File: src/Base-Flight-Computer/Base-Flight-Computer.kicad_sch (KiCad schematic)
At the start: 62 parts, among them J1 Jumper_NO, P1 1984659, P2 USB, P3 0530470610, P4 1546551-2, P5 1984659, Q1 QS5U17TR, Q2 2N7002W-7-F, Q3 2N7002W-7-F, Q4 QS5U17TR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

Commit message: updated symbol footprint links in schematic
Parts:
- BZ1: footprint Flight-Computer:AT-1438-TWT-R -> Base-Flight-Computer:AT-1438-TWT-R
- D1: footprint (none) -> Base-Flight-Computer:CLMVC-FKA-CL1D1L71BB7C3C3
- J1: footprint Engine-Controller:Jumper-NO -> Base-Flight-Computer:Jumper-NO
- P2: footprint Flight-Computer-Lite:10118194-0001LF -> Base-Flight-Computer:10118194-0001LF
- P3: footprint Flight-Computer-Lite:3220-20-0200-00 -> Base-Flight-Computer:53047-0610
- P4: footprint Flight-Computer:1546551-2 -> Base-Flight-Computer:1546551-2
- P5: footprint Base-Flight-Computer:JST_S2B-PH-K-S(LF)(SN) -> Base-Flight-Computer:1984659
- Q1, Q4: footprint Flight-Computer:QS5U17TR -> Base-Flight-Computer:QS5U17TR
- Q2, Q5, Q6: footprint Flight-Computer-Lite:QS5U17TR -> Base-Flight-Computer:2N7002W-7-F
- Q3: footprint Flight-Computer-Lite:QS5U17TR -> Base-Flight-Computer:QS5U17TR
- U1: footprint (none) -> Base-Flight-Computer:STM32G4A1KEU6
- U2: footprint (none) -> Base-Flight-Computer:BMP390
- U4: footprint (none) -> Base-Flight-Computer:SST25VF040B-50-4I-S2AE-T
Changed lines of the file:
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@@
       (effects (font (size 1.27 1.27)) (justify left) hide)
     )
-    (property "Footprint" "Flight-Computer-Lite:QS5U17TR" (at 221.361 58.293 0)
+    (property "Footprint" "Base-Flight-Computer:2N7002W-7-F" (at 221.361 58.293 0)
       (effects (font (size 1.27 1.27) italic) (justify left) hide)
     )
@@
       (effects (font (size 1.27 1.27)) (justify left) hide)
     )
-    (property "Footprint" "Flight-Computer-Lite:QS5U17TR" (at 270.637 59.182 0)
+    (property "Footprint" "Base-Flight-Computer:2N7002W-7-F" (at 270.637 59.182 0)
       (effects (font (size 1.27 1.27) italic) (justify left) hide)
     )
@@
       (effects (font (size 1.27 1.27)))
     )
-    (property "Footprint" "" (at 52.578 112.268 0)
+    (property "Footprint" "Base-Flight-Computer:BMP390" (at 52.578 112.268 0)
       (effects (font (size 1.27 1.27)) (justify left bottom) hide)
     )
@@
       (effects (font (size 1.524 1.524)) hide)
     )
-    (property "Footprint" "" (at 32.893 25.273 0)
+    (property "Footprint" "Base-Flight-Computer:STM32G4A1KEU6" (at 32.893 25.273 0)
       (effects (font (size 1.27 1.27) italic) hide)
     )
@@
       (effects (font (size 1.524 1.524)) hide)
     )
-    (property "Footprint" "Base-Flight-Computer:JST_S2B-PH-K-S(LF)(SN)" (at 31.115 166.37 0)
+    (property "Footprint" "Base-Flight-Computer:1984659" (at 31.115 166.37 0)
       (effects (font (size 1.524 1.524)) hide)
     )
@@
       (effects (font (size 1.27 1.27)) (justify left) hide)
     )
-    (property "Footprint" "Flight-Computer:QS5U17TR" (at 191.77 108.839 0)
+    (property "Footprint" "Base-Flight-Computer:QS5U17TR" (at 191.77 108.839 0)
       (effects (font (size 1.27 1.27) italic) (justify left) hide)
     )
@@
       (effects (font (size 1.27 1.27)) hide)
     )
-    (property "Footprint" "Engine-Controller:Jumper-NO" (at 140.97 149.606 0)
+    (property "Footprint" "Base-Flight-Computer:Jumper-NO" (at 140.97 149.606 0)
       (effects (font (size 1.27 1.27)) hide)
     )
@@
       (effects (font (size 1.524 1.524)) hide)
     )
-    (property "Footprint" "Flight-Computer:1546551-2" (at 31.115 179.578 0)
+    (property "Footprint" "Base-Flight-Computer:1546551-2" (at 31.115 179.578 0)
       (effects (font (size 1.524 1.524)) hide)
     )
@@
       (effects (font (size 1.27 1.27)) (justify left) hide)
     )
-    (property "Footprint" "Flight-Computer-Lite:QS5U17TR" (at 225.425 107.315 0)
+    (property "Footprint" "Base-Flight-Computer:QS5U17TR" (at 225.425 107.315 0)
       (effects (font (size 1.27 1.27) italic) (justify left) hide)
     )
@@
       (effects (font (size 1.27 1.27)) (justify left bottom) hide)
     )
-    (property "Footprint" "Flight-Computer-Lite:10118194-0001LF" (at 131.191 134.874 0)
+    (property "Footprint" "Base-Flight-Computer:10118194-0001LF" (at 131.191 134.874 0)
       (effects (font (size 1.27 1.27)) (justify left bottom) hide)
     )
@@
       (effects (font (size 1.27 1.27)) (justify left) hide)
     )
-    (property "Footprint" "Flight-Computer-Lite:QS5U17TR" (at 265.303 110.998 0)
+    (property "Footprint" "Base-Flight-Computer:2N7002W-7-F" (at 265.303 110.998 0)
       (effects (font (size 1.27 1.27) italic) (justify left) hide)
     )
@@
       (effects (font (size 1.27 1.27)) (justify left) hide)
     )
-    (property "Footprint" "Flight-Computer:AT-1438-TWT-R" (at 268.859 81.153 90)
+    (property "Footprint" "Base-Flight-Computer:AT-1438-TWT-R" (at 268.859 81.153 90)
       (effects (font (size 1.27 1.27)) hide)
     )
@@
       (effects (font (size 1.524 1.524)) hide)
     )
-    (property "Footprint" "Flight-Computer-Lite:3220-20-0200-00" (at 99.06 204.724 0)
+    (property "Footprint" "Base-Flight-Computer:53047-0610" (at 99.06 204.724 0)
       (effects (font (size 1.524 1.524)) hide)
     )
@@
       (effects (font (size 1.27 1.27)) (justify left bottom) hide)
     )
-    (property "Footprint" "" (at 136.017 75.565 0)
+    (property "Footprint" "Base-Flight-Computer:CLMVC-FKA-CL1D1L71BB7C3C3" (at 136.017 75.565 0)
       (effects (font (size 1.27 1.27)) (justify left bottom) hide)
     )
@@
       (effects (font (size 1.27 1.27)) (justify left) hide)
     )
-    (property "Footprint" "Flight-Computer:QS5U17TR" (at 191.897 58.166 0)
+    (property "Footprint" "Base-Flight-Computer:QS5U17TR" (at 191.897 58.166 0)
       (effects (font (size 1.27 1.27) italic) (justify left) hide)
     )
@@
       (effects (font (size 1.524 1.524)) hide)
     )
-    (property "Footprint" "" (at 205.359 153.797 0)
-      (effects (font (size 1.524 1.524)) hide)
-    )
+    (property "Footprint" "Base-Flight-Computer:SST25VF040B-50-4I-S2AE-T" (at 205.359 153.797 0)
+      (effects (font (size 1.524 1.524)) hide)
+    )

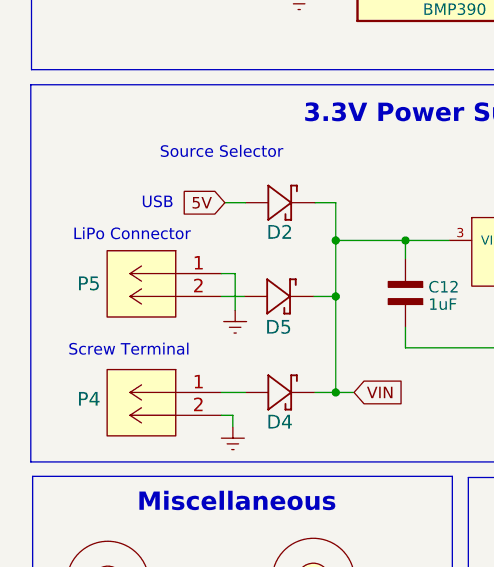
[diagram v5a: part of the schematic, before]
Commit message: added four terminal screw terminal to lib files
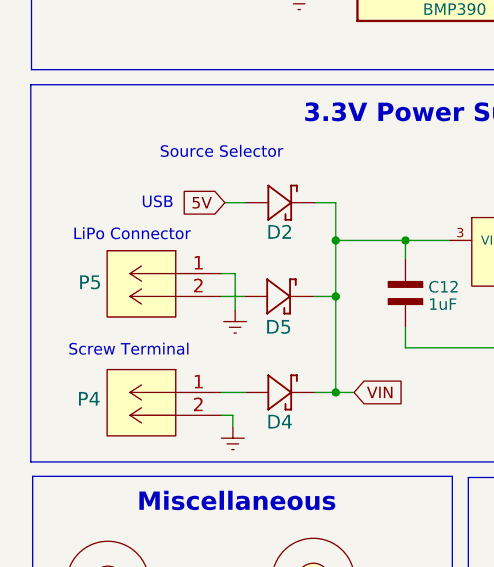
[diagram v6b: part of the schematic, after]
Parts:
- P5: footprint Base-Flight-Computer:1984659 -> Base-Flight-Computer:JST_S2B-PH-K-S(LF)(SN)
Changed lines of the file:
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@@
-    )
-  )
-  (symbol (lib_id "Base-Flight-Computer:S2B-PH-K-S__LF__SN") (at 34.925 135.89 0) (mirror y) (unit 1)
-    (in_bom yes) (on_board yes) (dnp no)
-    (property "Reference" "P5" (at 20.193 137.033 0)
-      (effects (font (size 1.524 1.524)))
-    )
-    (property "Value" "1984659" (at 29.845 163.83 0)
-      (effects (font (size 1.524 1.524)) hide)
-    )
-    (property "Footprint" "Base-Flight-Computer:1984659" (at 31.115 166.37 0)
-      (effects (font (size 1.524 1.524)) hide)
-    )
-    (property "Datasheet" "" (at 34.925 135.89 0)
-      (effects (font (size 1.524 1.524)) hide)
-    )
-    (pin "1")
-    (pin "2")
-    (instances
-      (project "Base-Flight-Computer"
-        (path "/13f33ffc-3ab1-449a-9be0-c2c7f72f3b48"
-          (reference "P5") (unit 1)
-        )
-      )
     )
   )
@@
         )
       )
+    )
+  )
+  (symbol (lib_id "Base-Flight-Computer:S2B-PH-K-S__LF__SN") (at 34.925 135.89 0) (mirror y) (unit 1)
+    (in_bom yes) (on_board yes) (dnp no)
+    (property "Reference" "P5" (at 20.32 136.906 0)
+      (effects (font (size 1.524 1.524)))
+    )
+    (property "Value" "1984659" (at 29.845 163.83 0)
+      (effects (font (size 1.524 1.524)) hide)
+    )
+    (property "Footprint" "Base-Flight-Computer:JST_S2B-PH-K-S(LF)(SN)" (at 31.115 166.37 0)
+      (effects (font (size 1.524 1.524)) hide)
+    )
+    (property "Datasheet" "" (at 34.925 135.89 0)
+      (effects (font (size 1.524 1.524)) hide)
+    )
+    (pin "1")
+    (pin "2")
+    (instances
+      (project "Base-Flight-Computer"
+        (path "/13f33ffc-3ab1-449a-9be0-c2c7f72f3b48"
+          (reference "P5") (unit 1)
+        )
+      )

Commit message: replaced green power indication LED with smaller 0603 alternate
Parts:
- removed D3: SML-LX1206GC-TR, Flight-Computer:SML-LX1206GC-TR, symbol Flight-Computer:SML-LX1206GC-TR
- removed P1: 1984659, Base-Flight-Computer:1984659, symbol Base-Flight-Computer:284391-6
- removed P4: 1546551-2, Base-Flight-Computer:1546551-2, symbol Flight-Computer:1546551-2
- added D3: LTST-C191KGKT, Base-Flight-Computer:LTST-C191KGKT, symbol Base-Flight-Computer:LTST-C191KGKT
- added P1, P4: 1984659, Base-Flight-Computer:1546551-4, symbol Base-Flight-Computer:1546551-4
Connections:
- net 3.3V: now also D3.2
- net Earth: now also P1.2 (6)
- net VIN: now also P4.3 (5)
- net VIN_SW: now also P1.3 (5), P4.1 (5), P4.4 (6)
- net at Q1.5 (D), Q2.1 (G), R3.2: now also P1.4 (6)
- net at R16.2: now also D3.1
- net at Q3.1 (G), Q4.5 (D), R9.2: now also P4.2 (6)
- net at D4.2: now also P1.1 (5)

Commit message: replaced schottky diode with smaller form factor diode
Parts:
- removed D2, D4, D5: SM5819PL-TP, Base-Flight-Computer:SM5819PL-TP, symbol Base-Flight-Computer:SM5819PL-TP
- added D2, D4, D5: PMEG3010AESBYL, Base-Flight-Computer:PMEG3010AESBYL, symbol Base-Flight-Computer:PMEG3010AESBYL
- Q3: footprint Base-Flight-Computer:QS5U17TR -> Base-Flight-Computer:2N7002W-7-F
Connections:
- net 5V: now also D2.A
- net VIN: now also D2.C, D4.C, D5.C
- net at P5.2 (6): now also D5.A
- net at P1.1 (5): now also D4.A
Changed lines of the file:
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@@
   (junction (at 221.996 35.814) (diameter 0) (color 0 0 0 0)
   )
-  (junction (at 47.625 149.098) (diameter 0) (color 0 0 0 0)
-  )
   (junction (at 134.239 124.714) (diameter 0) (color 0 0 0 0)
   )
@@
   (junction (at 132.715 35.433) (diameter 0) (color 0 0 0 0)
   )
+  (junction (at 47.625 149.098) (diameter 0) (color 0 0 0 0)
+  )
   (junction (at 55.372 132.207) (diameter 0) (color 0 0 0 0)
   )
@@
     (stroke (width 0) (type default))
   )
-  (wire (pts (xy 45.339 149.098) (xy 47.625 149.098))
-    (stroke (width 0) (type default))
-  )
   (wire (pts (xy 88.9 190.5) (xy 86.868 190.5))
     (stroke (width 0) (type default))
@@
     (stroke (width 0) (type default))
   )
+  (wire (pts (xy 45.466 149.098) (xy 47.625 149.098))
+    (stroke (width 0) (type default))
+  )
   (wire (pts (xy 142.367 54.229) (xy 142.367 56.515))
     (stroke (width 0) (type default))
@@
     (stroke (width 0) (type default))
   )
+  (wire (pts (xy 34.798 149.098) (xy 37.719 149.098))
+    (stroke (width 0) (type default))
+  )
   (wire (pts (xy 215.519 144.907) (xy 217.805 144.907))
     (stroke (width 0) (type default))
@@
     (stroke (width 0) (type default))
   )
-  (wire (pts (xy 34.798 149.098) (xy 37.592 149.098))
-    (stroke (width 0) (type default))
-  )
   (wire (pts (xy 265.938 100.203) (xy 265.938 101.473))
     (stroke (width 0) (type default))
@@
     )
   )
+  (symbol (lib_id "Base-Flight-Computer:PMEG3010AESBYL") (at 41.402 128.016 0) (unit 1)
+    (in_bom yes) (on_board yes) (dnp no) (fields_autoplaced)
+    (property "Reference" "D2" (at 41.7195 125.0075 0)
+      (effects (font (size 1.524 1.524)))
+    )
+    (property "Value" "PMEG3010AESBYL" (at 42.672 133.096 0)
+      (effects (font (size 1.524 1.524)) hide)
+    )
+    (property "Footprint" "Base-Flight-Computer:PMEG3010AESBYL" (at 42.672 135.636 0)
+      (effects (font (size 1.524 1.524)) hide)
+    )
+    (property "Datasheet" "" (at 36.322 128.016 0)
+      (effects (font (size 1.524 1.524)) hide)
+    )
+    (pin "A")
+    (pin "C")
+    (instances
+      (project "Base-Flight-Computer"
+        (path "/13f33ffc-3ab1-449a-9be0-c2c7f72f3b48"
+          (reference "D2") (unit 1)
+        )
+      )
+    )
+  )
   (symbol (lib_id "Flight-Computer:Earth") (at 69.088 145.923 0) (unit 1)
     (in_bom yes) (on_board yes) (dnp no) (fields_autoplaced)
@@
     )
   )
+  (symbol (lib_id "Base-Flight-Computer:PMEG3010AESBYL") (at 41.275 138.43 0) (unit 1)
+    (in_bom yes) (on_board yes) (dnp no) (fields_autoplaced)
+    (property "Reference" "D5" (at 41.5925 135.4215 0)
+      (effects (font (size 1.524 1.524)))
+    )
+    (property "Value" "PMEG3010AESBYL" (at 42.545 143.51 0)
+      (effects (font (size 1.524 1.524)) hide)
+    )
+    (property "Footprint" "Base-Flight-Computer:PMEG3010AESBYL" (at 42.545 146.05 0)
+      (effects (font (size 1.524 1.524)) hide)
+    )
+    (property "Datasheet" "" (at 36.195 138.43 0)
+      (effects (font (size 1.524 1.524)) hide)
+    )
+    (pin "A")
+    (pin "C")
+    (instances
+      (project "Base-Flight-Computer"
+        (path "/13f33ffc-3ab1-449a-9be0-c2c7f72f3b48"
+          (reference "D5") (unit 1)
+        )
+      )
+    )
+  )
   (symbol (lib_id "Flight-Computer:Earth") (at 253.873 52.705 0) (unit 1)
     (in_bom yes) (on_board yes) (dnp no) (fields_autoplaced)
@@
     )
   )
+  (symbol (lib_id "Base-Flight-Computer:PMEG3010AESBYL") (at 41.529 149.098 0) (unit 1)
+    (in_bom yes) (on_board yes) (dnp no) (fields_autoplaced)
+    (property "Reference" "D4" (at 41.8465 146.0895 0)
+      (effects (font (size 1.524 1.524)))
+    )
+    (property "Value" "PMEG3010AESBYL" (at 42.799 154.178 0)
+      (effects (font (size 1.524 1.524)) hide)
+    )
+    (property "Footprint" "Base-Flight-Computer:PMEG3010AESBYL" (at 42.799 156.718 0)
+      (effects (font (size 1.524 1.524)) hide)
+    )
+    (property "Datasheet" "" (at 36.449 149.098 0)
+      (effects (font (size 1.524 1.524)) hide)
+    )
+    (pin "A")
+    (pin "C")
+    (instances
+      (project "Base-Flight-Computer"
+        (path "/13f33ffc-3ab1-449a-9be0-c2c7f72f3b48"
+          (reference "D4") (unit 1)
+        )
+      )
+    )
+  )
   (symbol (lib_id "Flight-Computer:Earth") (at 132.715 36.703 0) (unit 1)
     (in_bom yes) (on_board yes) (dnp no) (fields_autoplaced)
@@
     )
   )
-  (symbol (lib_id "Base-Flight-Computer:SM5819PL-TP") (at 41.275 138.43 0) (unit 1)
-    (in_bom yes) (on_board yes) (dnp no)
-    (property "Reference" "D5" (at 41.275 141.859 0)
-      (effects (font (size 1.524 1.524)))
-    )
-    (property "Value" "SM5819PL-TP" (at 42.545 143.51 0)
-      (effects (font (size 1.524 1.524)) hide)
-    )
-    (property "Footprint" "Base-Flight-Computer:SM5819PL-TP" (at 42.545 146.05 0)
-      (effects (font (size 1.524 1.524)) hide)
-    )
-    (property "Datasheet" "" (at 36.195 138.43 0)
-      (effects (font (size 1.524 1.524)) hide)
-    )
-    (pin "1")
-    (pin "2")
-    (instances
-      (project "Base-Flight-Computer"
-        (path "/13f33ffc-3ab1-449a-9be0-c2c7f72f3b48"
-          (reference "D5") (unit 1)
-        )
-      )
-    )
-  )
   (symbol (lib_id "Base-Flight-Computer:RES_0402") (at 226.06 80.137 90) (unit 1)
     (in_bom yes) (on_board yes) (dnp no) (fields_autoplaced)
@@
     )
   )
-  (symbol (lib_id "Base-Flight-Computer:SM5819PL-TP") (at 41.402 149.098 0) (unit 1)
-    (in_bom yes) (on_board yes) (dnp no)
-    (property "Reference" "D4" (at 41.402 152.4 0)
-      (effects (font (size 1.524 1.524)))
-    )
-    (property "Value" "SM5819PL-TP" (at 42.672 154.178 0)
-      (effects (font (size 1.524 1.524)) hide)
-    )
-    (property "Footprint" "Base-Flight-Computer:SM5819PL-TP" (at 42.672 156.718 0)
-      (effects (font (size 1.524 1.524)) hide)
-    )
-    (property "Datasheet" "" (at 36.322 149.098 0)
-      (effects (font (size 1.524 1.524)) hide)
-    )
-    (pin "1")
-    (pin "2")
-    (instances
-      (project "Base-Flight-Computer"
-        (path "/13f33ffc-3ab1-449a-9be0-c2c7f72f3b48"
-          (reference "D4") (unit 1)
-        )
-      )
-    )
-  )
   (symbol (lib_id "Flight-Computer:Earth") (at 266.065 150.241 0) (unit 1)
     (in_bom yes) (on_board yes) (dnp no) (fields_autoplaced)
@@
       (effects (font (size 1.27 1.27)) (justify left) hide)
     )
-    (property "Footprint" "Base-Flight-Computer:QS5U17TR" (at 225.425 107.315 0)
+    (property "Footprint" "Base-Flight-Computer:2N7002W-7-F" (at 225.425 107.315 0)
       (effects (font (size 1.27 1.27) italic) (justify left) hide)
     )
@@
         )
       )
-    )
-  )
-  (symbol (lib_id "Base-Flight-Computer:SM5819PL-TP") (at 41.402 128.016 0) (unit 1)
-    (in_bom yes) (on_board yes) (dnp no)
-    (property "Reference" "D2" (at 41.402 131.318 0)
-      (effects (font (size 1.524 1.524)))
-    )
-    (property "Value" "SM5819PL-TP" (at 42.672 133.096 0)
-      (effects (font (size 1.524 1.524)) hide)
-    )
-    (property "Footprint" "Base-Flight-Computer:SM5819PL-TP" (at 42.672 135.636 0)
-      (effects (font (size 1.524 1.524)) hide)
-    )
-    (property "Datasheet" "" (at 36.322 128.016 0)
-      (effects (font (size 1.524 1.524)) hide)
-    )
-    (pin "1")
-    (pin "2")
-    (instances
-      (project "Base-Flight-Computer"
-        (path "/13f33ffc-3ab1-449a-9be0-c2c7f72f3b48"
-          (reference "D2") (unit 1)
-        )
-      )
